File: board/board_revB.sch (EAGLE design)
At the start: 67 parts, among them Q1 ULN2003AS, Q2 ULN2003AD, Y1 8Mhz

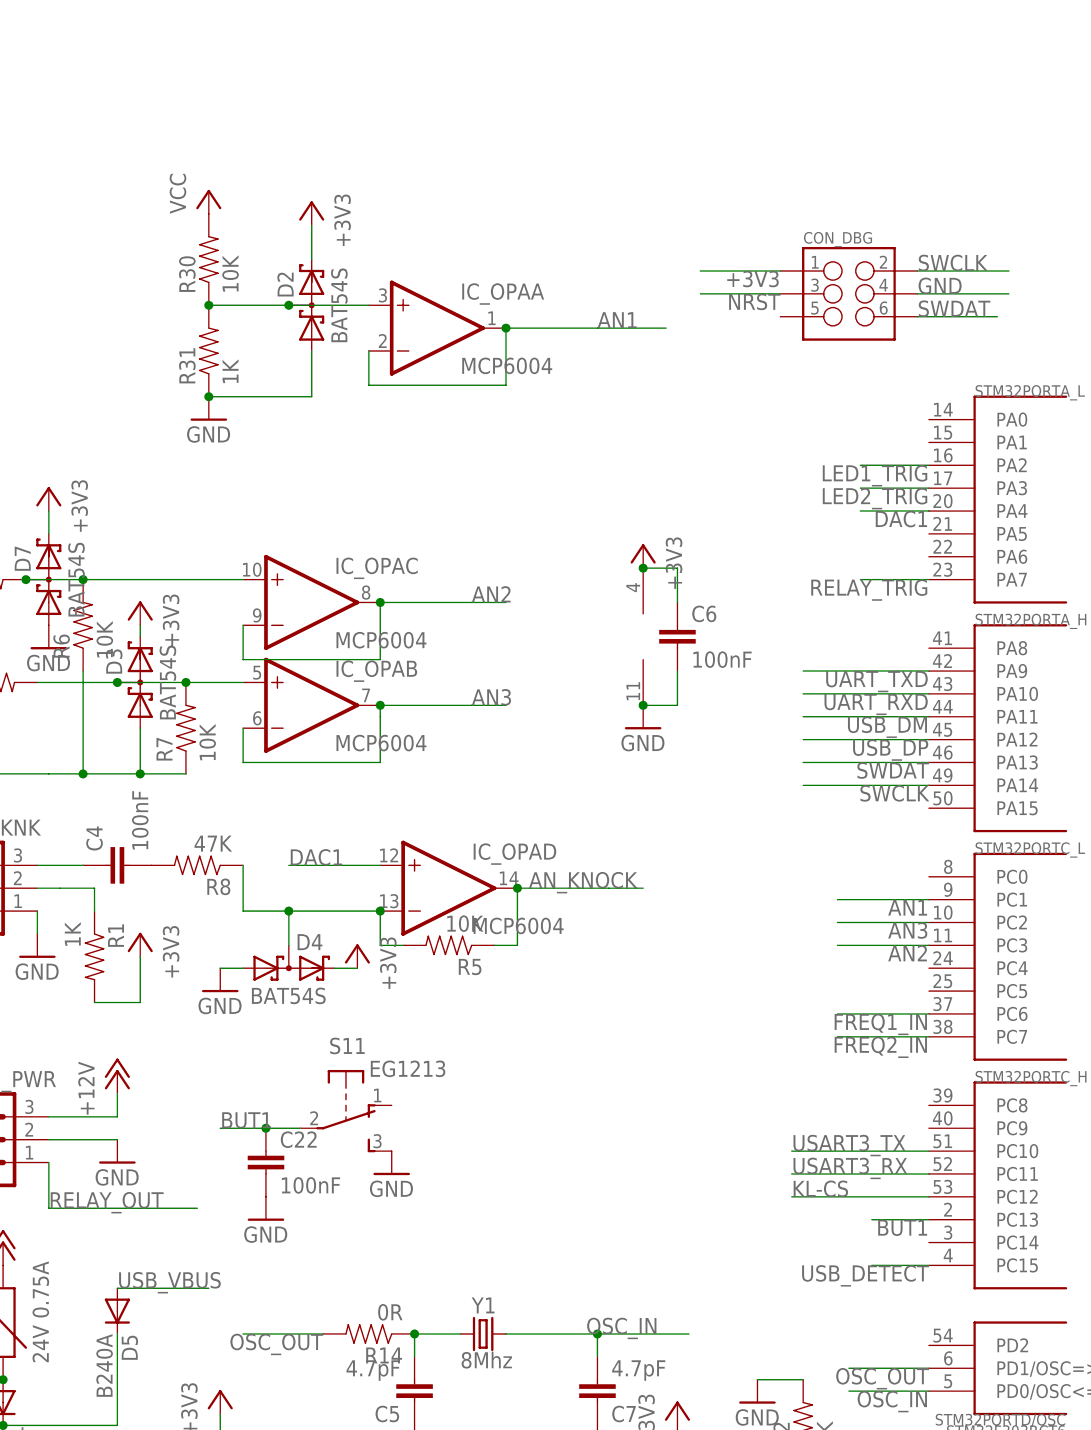
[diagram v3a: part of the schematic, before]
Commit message: [Board Rev B] Adding another switch
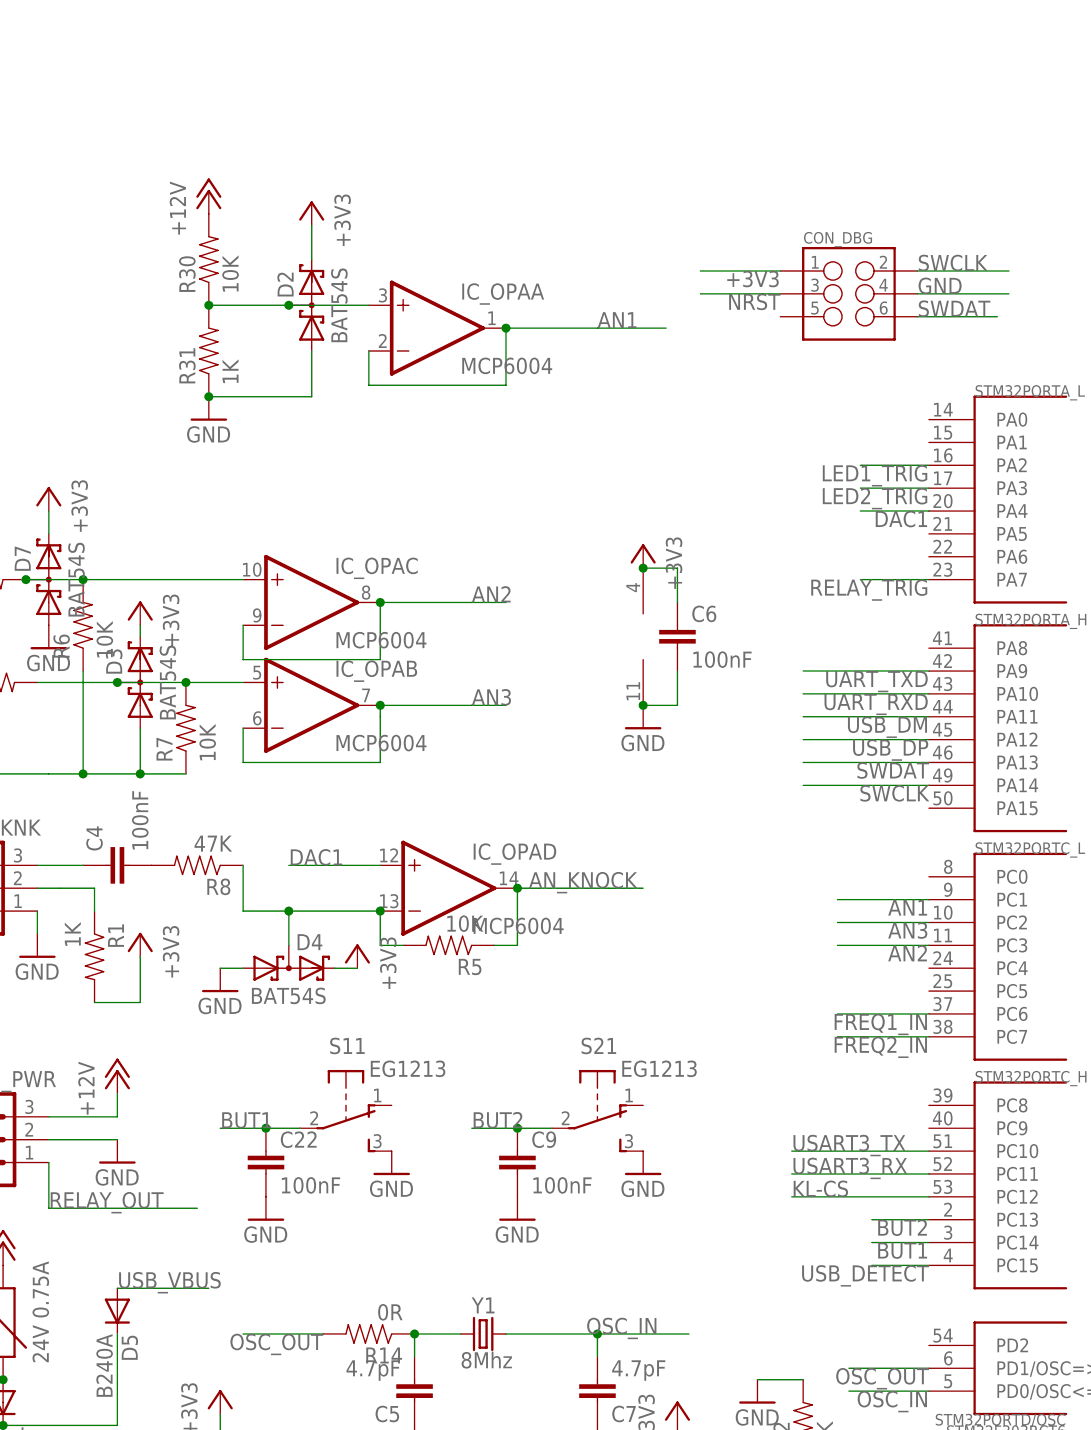
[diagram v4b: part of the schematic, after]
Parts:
- added C9: 100nF, SparkFun-Capacitors:CAP0603-CAP
- added S2: EG1213, adafruit:EG1213
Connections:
- new net BUT2: C9.1, S21.P, STM32PORTC_H.PC13
- net +12V: now also R30.2
- net BUT1: now also STM32PORTC_H.PC14; no longer STM32PORTC_H.PC13
- net GND: now also C9.2, S21.S
- net VCC: no longer R30.2
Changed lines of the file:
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@@
 <part name="R31" library="SparkFun-Resistors" deviceset="RESISTOR" device="0603-RES" value="1K"/>
 <part name="GND34" library="supply1" deviceset="GND" device=""/>
-<part name="P+10" library="supply1" deviceset="VCC" device=""/>
 <part name="R32" library="SparkFun-Resistors" deviceset="RESISTOR" device="0603-RES" value="10K"/>
 <part name="C34" library="SparkFun-Passives" deviceset="CAP" device="0603-CAP" value="4.7uF"/>
@@
 <part name="CON_UART" library="SparkFun-Connectors" deviceset="M03" device="PTH"/>
 <part name="GND22" library="supply1" deviceset="GND" device=""/>
+<part name="GND24" library="supply1" deviceset="GND" device=""/>
+<part name="C9" library="SparkFun-Capacitors" deviceset="CAP" device="0603-CAP" value="100nF"/>
+<part name="GND25" library="supply1" deviceset="GND" device=""/>
+<part name="S2" library="adafruit" deviceset="EG1213" device=""/>
+<part name="P+5" library="supply1" deviceset="+12V" device=""/>
 </parts>
 <sheets>
@@
 <instance part="R31" gate="G$1" x="62.23" y="146.05" rot="R90"/>
 <instance part="GND34" gate="1" x="62.23" y="138.43"/>
-<instance part="P+10" gate="VCC" x="62.23" y="163.83"/>
 <instance part="R32" gate="G$1" x="36.83" y="120.65"/>
 <instance part="C34" gate="G$1" x="74.93" y="17.78"/>
@@
 <instance part="CON_UART" gate="G$1" x="285.75" y="156.21"/>
 <instance part="GND22" gate="1" x="293.37" y="151.13"/>
+<instance part="GND24" gate="1" x="110.49" y="54.61"/>
+<instance part="C9" gate="G$1" x="96.52" y="54.61"/>
+<instance part="GND25" gate="1" x="96.52" y="49.53"/>
+<instance part="S2" gate="1" x="105.41" y="59.69" rot="R270"/>
+<instance part="P+5" gate="1" x="62.23" y="163.83"/>
 </instances>
 <busses>
@@
 <pinref part="GND22" gate="1" pin="GND"/>
 </segment>
+<segment>
+<pinref part="C9" gate="G$1" pin="2"/>
+<pinref part="GND25" gate="1" pin="GND"/>
+</segment>
+<segment>
+<pinref part="S2" gate="1" pin="S"/>
+<pinref part="GND24" gate="1" pin="GND"/>
+</segment>
 </net>
 <net name="+3V3" class="0">
@@
 <pinref part="P+2" gate="1" pin="+12V"/>
 <pinref part="F1" gate="G$1" pin="2"/>
+</segment>
+<segment>
+<pinref part="R30" gate="G$1" pin="2"/>
+<pinref part="P+5" gate="1" pin="+12V"/>
 </segment>
 </net>
@@
 <wire x1="39.37" y1="26.67" x2="33.02" y2="26.67" width="0.1524" layer="91"/>
 </segment>
-<segment>
-<pinref part="R30" gate="G$1" pin="2"/>
-<pinref part="P+10" gate="VCC" pin="VCC"/>
-</segment>
 </net>
 <net name="BOOT0" class="0">
@@
 </segment>
 <segment>
-<wire x1="142.24" y1="49.53" x2="135.89" y2="49.53" width="0.1524" layer="91"/>
-<label x="142.24" y="49.53" size="1.778" layer="95" rot="R180"/>
-<pinref part="STM32" gate="PORTC_H" pin="PC13"/>
+<pinref part="STM32" gate="PORTC_H" pin="PC14"/>
+<wire x1="142.24" y1="46.99" x2="135.89" y2="46.99" width="0.1524" layer="91"/>
+<label x="142.24" y="46.99" size="1.778" layer="95" rot="R180"/>
 </segment>
 </net>
@@
 </segment>
 </net>
+<net name="BUT2" class="0">
+<segment>
+<wire x1="100.33" y1="59.69" x2="96.52" y2="59.69" width="0.1524" layer="91"/>
+<label x="91.44" y="59.69" size="1.778" layer="95"/>
+<pinref part="C9" gate="G$1" pin="1"/>
+<wire x1="96.52" y1="59.69" x2="91.44" y2="59.69" width="0.1524" layer="91"/>
+<junction x="96.52" y="59.69"/>
+<pinref part="S2" gate="1" pin="P"/>
+</segment>
+<segment>
+<wire x1="142.24" y1="49.53" x2="135.89" y2="49.53" width="0.1524" layer="91"/>
+<label x="142.24" y="49.53" size="1.778" layer="95" rot="R180"/>
+<pinref part="STM32" gate="PORTC_H" pin="PC13"/>
+</segment>
+</net>

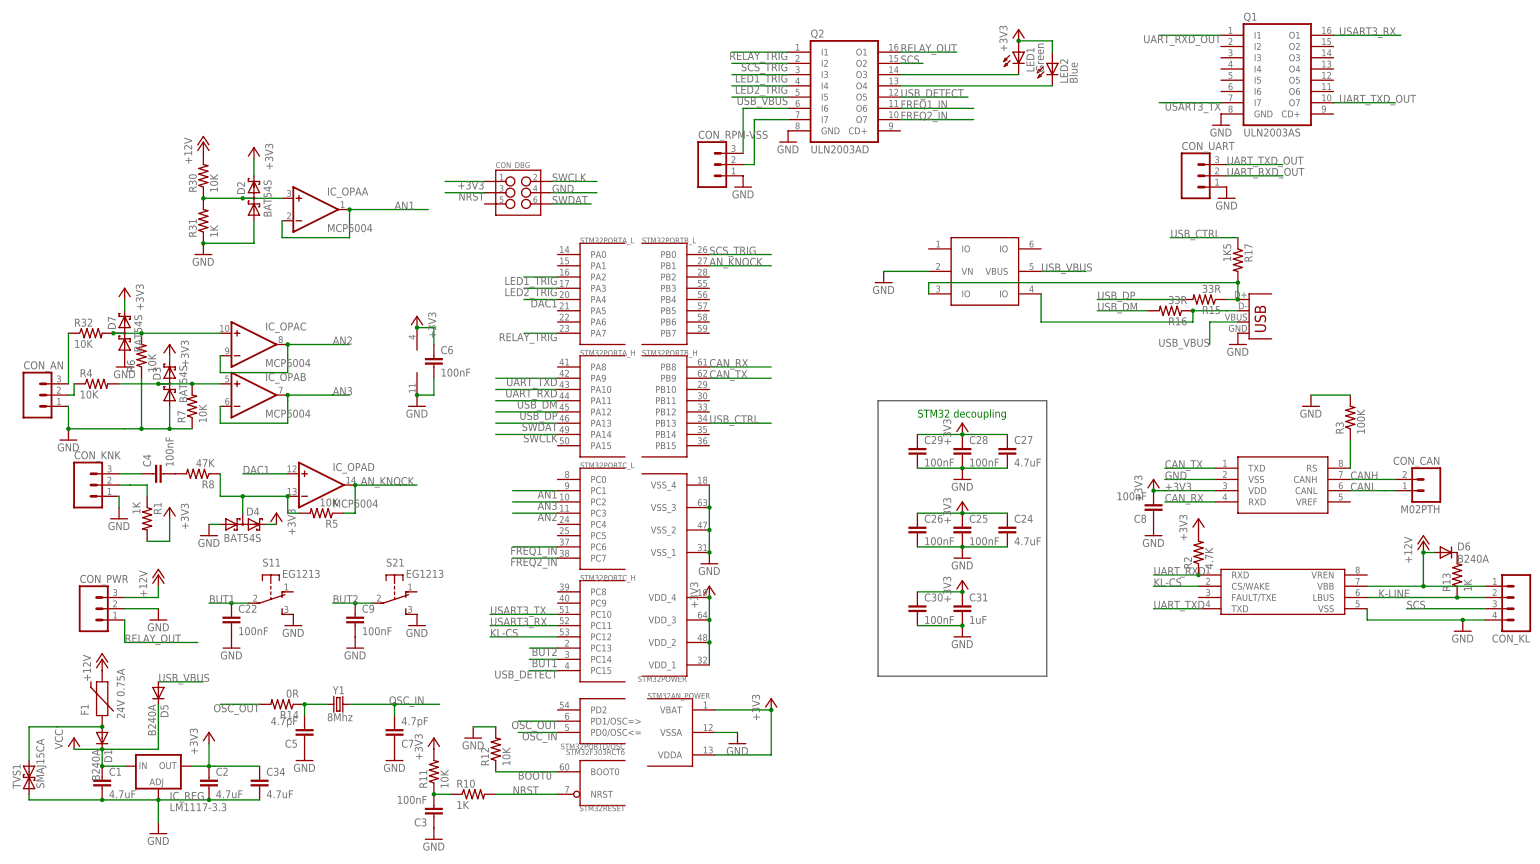
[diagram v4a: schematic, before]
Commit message: [Board Rev B] Multiple improvements. Adding extra UART.
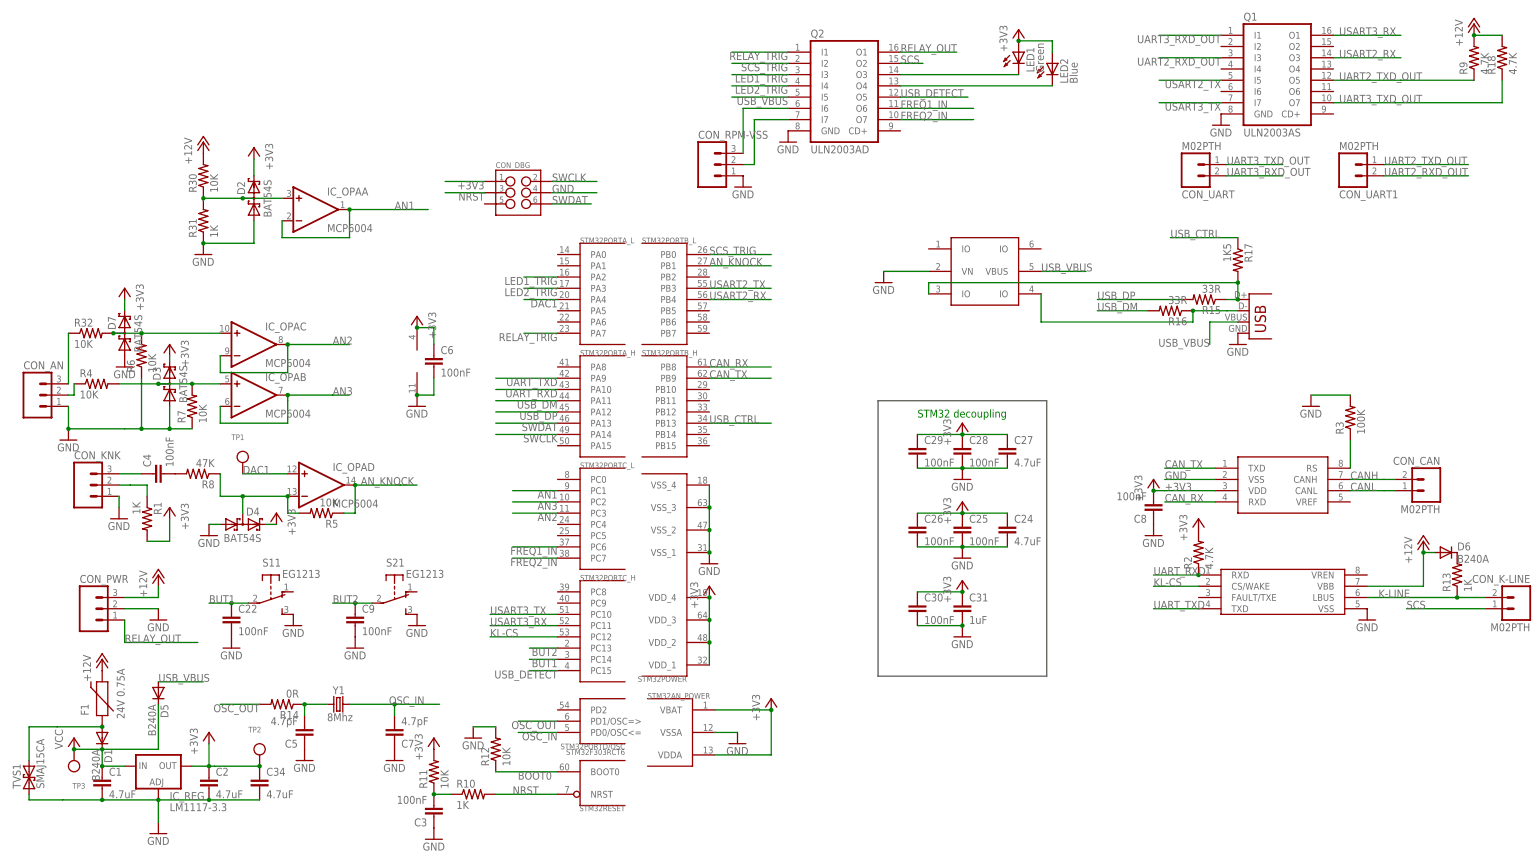
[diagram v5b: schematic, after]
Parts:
- removed CON_KL: (no value), SparkFun-Connectors:M04PTH
- added CON_K-LINE, CON_UART1: M02PTH, SparkFun-Connectors:M02PTH
- added R18, R9: 4.7K, SparkFun-Resistors:RESISTOR0603-RES
- added TP1, TP2, TP3: (no value), microbuilder:TESTPOINTROUND1MM
- CON_UART: value (none) -> M02PTH; device SparkFun-Connectors:M03PTH -> SparkFun-Connectors:M02PTH
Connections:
- net UART_RXD_OUT renamed UART3_RXD_OUT
- removed net UART_TXD_OUT: CON_UART.3, Q1.O7
- new net UART2_RXD_OUT: CON_UART1.2, Q1.I3
- new net UART2_TXD_OUT: CON_UART1.1, Q1.O5, R9.1
- new net UART3_TXD_OUT: CON_UART.1, Q1.O7, R18.1
- new net USART2_RX: Q1.O3, STM32PORTB_L.PB4
- new net USART2_TX: Q1.I5, STM32PORTB_L.PB3
- net +12V: now also R18.2, R9.2; no longer CON_KL.1
- net +3V3: now also TP2.P$1
- net DAC1: now also TP1.P$1
- net GND: no longer CON_KL.4, CON_UART.1
- net K-LINE: now also CON_K-LINE.2; no longer CON_KL.2
- net SCS: now also CON_K-LINE.1; no longer CON_KL.3
- net VCC: now also TP3.P$1

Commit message: [Board Rev B] Updating various components.
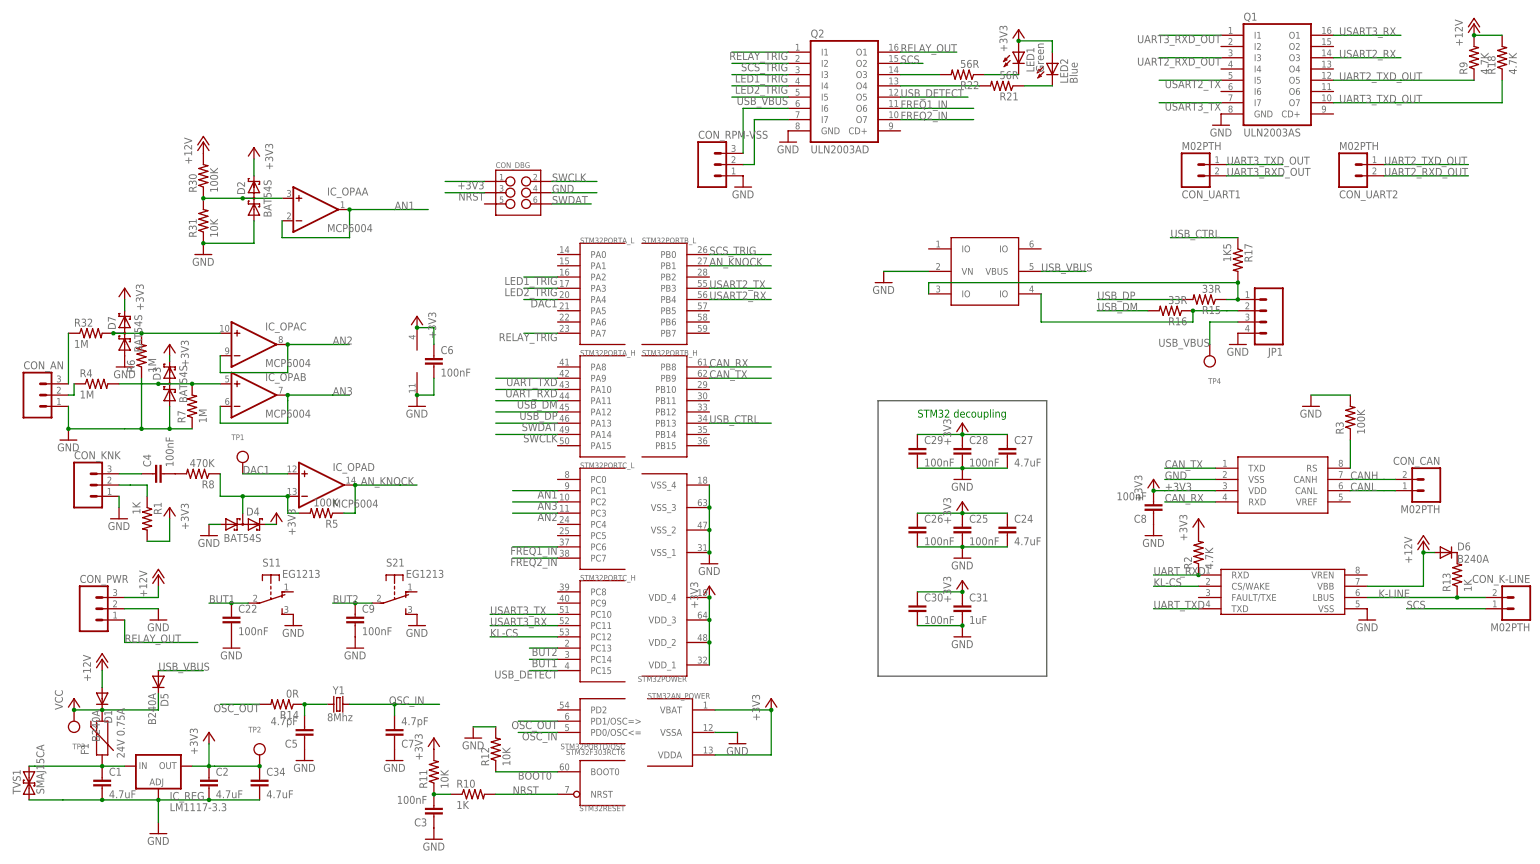
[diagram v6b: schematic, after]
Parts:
- removed CON_UART: M02PTH, SparkFun-Connectors:M02PTH
- removed CON_USB: USBSMD, SparkFun-Connectors:USBSMD
- added CON_UART2: M02PTH, SparkFun-Connectors:M02PTH
- added JP1: (no value), SparkFun-Connectors:M04LOCK
- added R21, R22: 56R, SparkFun-Resistors:RESISTOR0603-RES
- added TP4: (no value), microbuilder:TESTPOINTROUND1MM
- R30, R5: value 10K -> 100K
- R31: value 1K -> 10K
- R32, R4, R6, R7: value 10K -> 1M
- R8: value 47K -> 470K
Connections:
- removed net N$9: D1.A, F1.1, TVS1.2
- new net N$15: Q2.O3, R22.2
- new net N$19: LED1.C, R22.1
- new net N$20: C1.1, F1.1, IC_REG.IN, TVS1.2
- net +12V: now also D1.A; no longer F1.2
- net GND: now also JP1.4; no longer CON_USB.GND
- net N$10: now also LED2.C, R21.1; no longer LED1.C, Q2.O3
- net N$11: now also R21.2; no longer LED2.C
- net N$17: now also JP1.2; no longer CON_USB.D-
- net N$7: now also JP1.1; no longer CON_USB.D+
- net UART2_RXD_OUT: now also CON_UART2.2; no longer CON_UART1.2
- net UART2_TXD_OUT: now also CON_UART2.1; no longer CON_UART1.1
- net UART3_RXD_OUT: now also CON_UART1.2; no longer CON_UART.2
- net UART3_TXD_OUT: now also CON_UART1.1; no longer CON_UART.1
- net USB_VBUS: now also JP1.3, TP4.P$1; no longer CON_USB.VBUS
- net VCC: now also F1.2; no longer C1.1, IC_REG.IN
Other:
- moved on the sheet: CON_UART1, D1, D5, F1, TP3, TVS1
